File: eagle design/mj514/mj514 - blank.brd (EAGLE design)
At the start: 49 x 18 mm, 0 parts

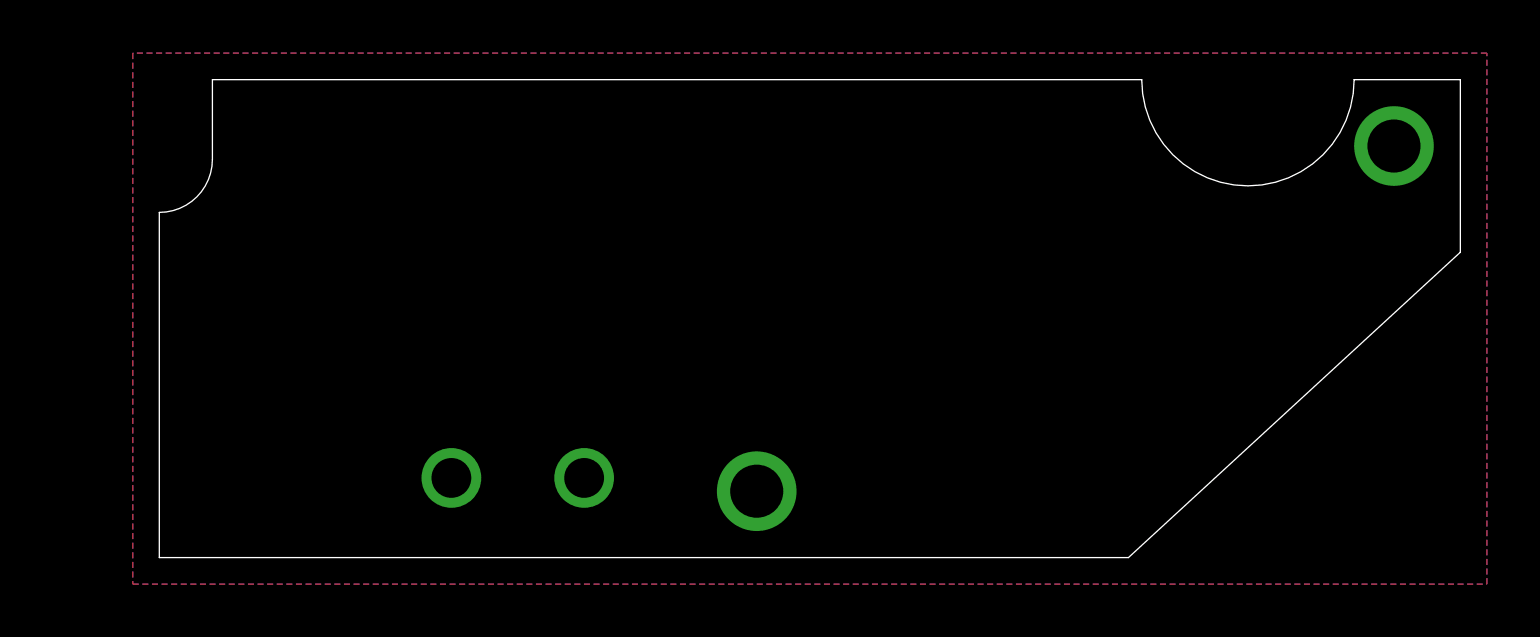
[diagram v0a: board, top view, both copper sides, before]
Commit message: added mj512 board outline - a slightly changed outline in respect to the original e14
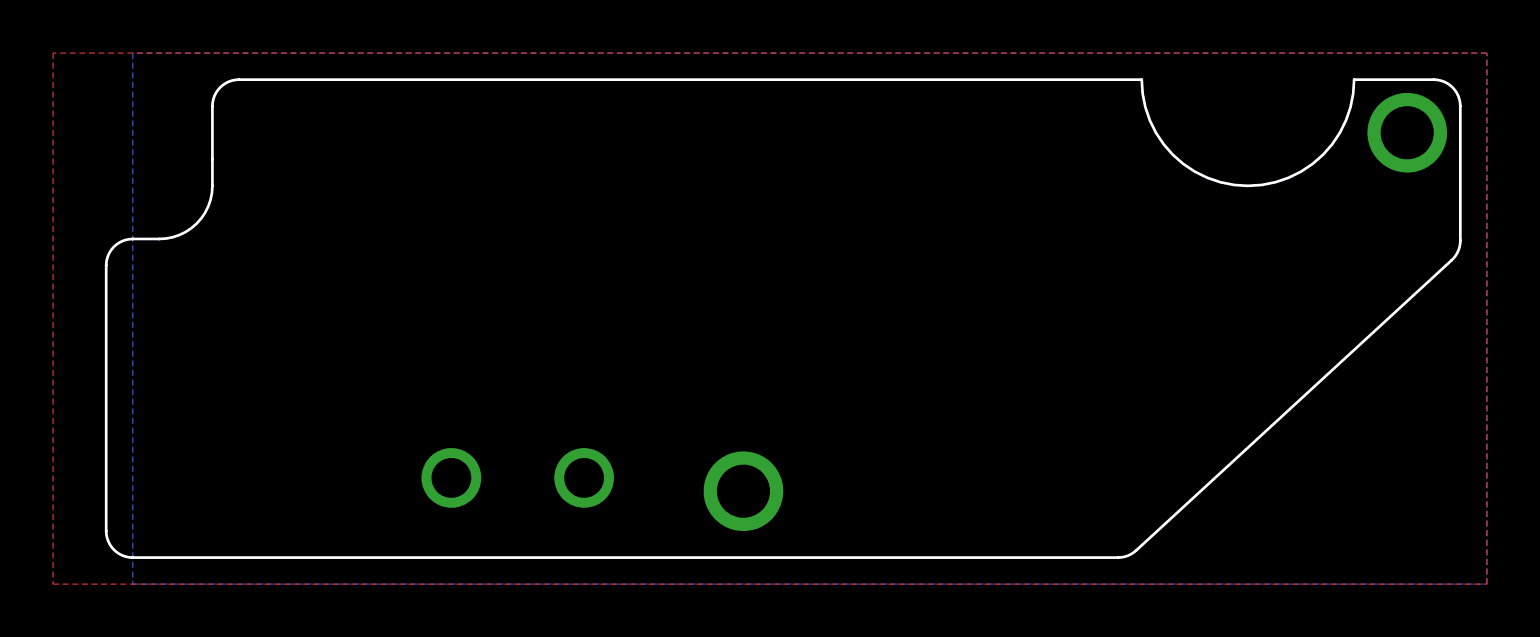
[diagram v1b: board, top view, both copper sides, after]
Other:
- board size 49 x 18 mm -> 51 x 18 mm
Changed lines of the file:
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@@
 <board>
 <plain>
-<wire x1="0" y1="0" x2="36.5" y2="0" width="0.01" layer="20"/>
-<wire x1="49" y1="11.5" x2="49" y2="18" width="0.01" layer="20"/>
-<wire x1="49" y1="18" x2="45" y2="18" width="0.01" layer="20"/>
-<wire x1="37" y1="18" x2="2" y2="18" width="0.01" layer="20"/>
+<wire x1="36.78703125" y1="0.26406875" x2="48.67705625" y2="11.202890625" width="0.1016" layer="20"/>
+<wire x1="48.67705625" y1="11.202890625" x2="49" y2="11.938821875" width="0.1016" layer="20" curve="47.385965"/>
+<wire x1="49" y1="11.938821875" x2="49" y2="17" width="0.1016" layer="20"/>
+<wire x1="49" y1="17" x2="48" y2="18" width="0.1016" layer="20" curve="90"/>
+<wire x1="48" y1="18" x2="45" y2="18" width="0.1016" layer="20"/>
+<wire x1="36.78703125" y1="0.26406875" x2="36.109975" y2="0" width="0.1016" layer="20" curve="-42.614035"/>
+<wire x1="36.109975" y1="0" x2="-1" y2="0" width="0.1016" layer="20"/>
+<wire x1="-1" y1="0" x2="-2" y2="1" width="0.1016" layer="20" curve="-90"/>
+<wire x1="-2" y1="1" x2="-2" y2="11" width="0.1016" layer="20"/>
+<wire x1="2" y1="15" x2="2" y2="17" width="0.1016" layer="20"/>
+<wire x1="2" y1="17" x2="3" y2="18" width="0.1016" layer="20" curve="-90"/>
+<wire x1="3" y1="18" x2="37" y2="18" width="0.1016" layer="20"/>
 <dimension x1="0" y1="-3" x2="49" y2="-3" x3="24.5" y3="-7" textsize="1.778" layer="47"/>
 <dimension x1="-3" y1="0" x2="-3" y2="18" x3="-7" y3="9" textsize="1.778" layer="47"/>
 <dimension x1="0" y1="-3" x2="36.5" y2="-3" x3="18.25" y3="-4" textsize="1.778" layer="47"/>
 <dimension x1="52" y1="18" x2="52" y2="11.5" x3="54" y3="14.75" textsize="1.778" layer="47"/>
-<wire x1="0" y1="13" x2="0" y2="0" width="0.01" layer="20"/>
-<wire x1="49" y1="11.5" x2="36.5" y2="0" width="0.01" layer="20"/>
+<wire x1="-2" y1="11" x2="-1" y2="12" width="0.1016" layer="20" curve="-90"/>
+<wire x1="-1" y1="12" x2="0" y2="12" width="0.1016" layer="20"/>
+<wire x1="0" y1="12" x2="2" y2="14" width="0.1016" layer="20" curve="90"/>
+<wire x1="2" y1="14" x2="2" y2="15" width="0.1016" layer="20"/>
 <dimension x1="0" y1="-11" x2="22.5" y2="-11" x3="11.25" y3="-13" textsize="1.778" layer="47"/>
-<wire x1="37" y1="18" x2="45" y2="18" width="0.01" layer="20" curve="180"/>
-<wire x1="2" y1="15" x2="2" y2="18" width="0.01" layer="20"/>
-<wire x1="2" y1="15" x2="0" y2="13" width="0.01" layer="20" curve="-90"/>
+<wire x1="37" y1="18" x2="45" y2="18" width="0.1016" layer="20" curve="180"/>
 <dimension x1="41" y1="18" x2="39.735090625" y2="14.20526875" x3="37.268515625" y3="6.8055375" textsize="1.778" layer="47" dtype="radius"/>
 <dimension x1="0" y1="22" x2="27.5" y2="22" x3="35.3" y3="22" textsize="1.778" layer="22" dtype="radius"/>
@@
 <signals>
 <signal name="GND">
-<via x="22.5" y="2.5" extent="1-16" drill="2"/>
-<via x="46.5" y="15.5" extent="1-16" drill="2"/>
+<via x="22" y="2.5" extent="1-16" drill="2"/>
+<via x="47" y="16" extent="1-16" drill="2"/>
 <polygon width="0.25" layer="1">
-<vertex x="-1" y="-1"/>
+<vertex x="-4" y="-1"/>
 <vertex x="50" y="-1"/>
 <vertex x="50" y="19"/>
-<vertex x="-1" y="19"/>
+<vertex x="-4" y="19"/>
 </polygon>
 <polygon width="0.25" layer="16">
